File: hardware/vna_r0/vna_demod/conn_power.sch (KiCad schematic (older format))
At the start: 7 parts

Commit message: work on vna r0 schematics
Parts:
- added C? (x2): 22 uF, symbol CP_Small
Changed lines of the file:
@@
 LIBS:conn_sma_2gnd
 LIBS:conn_sma
+LIBS:txco
+LIBS:nb3n551
+LIBS:hmc475
+LIBS:trf37b73
 LIBS:vna_demod-cache
 EELAYER 25 0
@@
 Wire Wire Line
 	7300 4000 7500 4000
+$Comp
+L CP_Small C?
+U 1 1 5940338C
+P 5650 5000
+F 0 "C?" H 5660 5070 50  0000 L CNN
+F 1 "22 uF" H 5660 4920 50  0000 L CNN
+F 2 "" H 5650 5000 50  0001 C CNN
+F 3 "" H 5650 5000 50  0001 C CNN
+	1    5650 5000
+	1    0    0    -1
+$EndComp
+$Comp
+L CP_Small C?
+U 1 1 59403410
+P 6200 5000
+F 0 "C?" H 6210 5070 50  0000 L CNN
+F 1 "22 uF" H 6210 4920 50  0000 L CNN
+F 2 "" H 6200 5000 50  0001 C CNN
+F 3 "" H 6200 5000 50  0001 C CNN
+	1    6200 5000
+	1    0    0    -1
+$EndComp
 $EndSCHEMATC

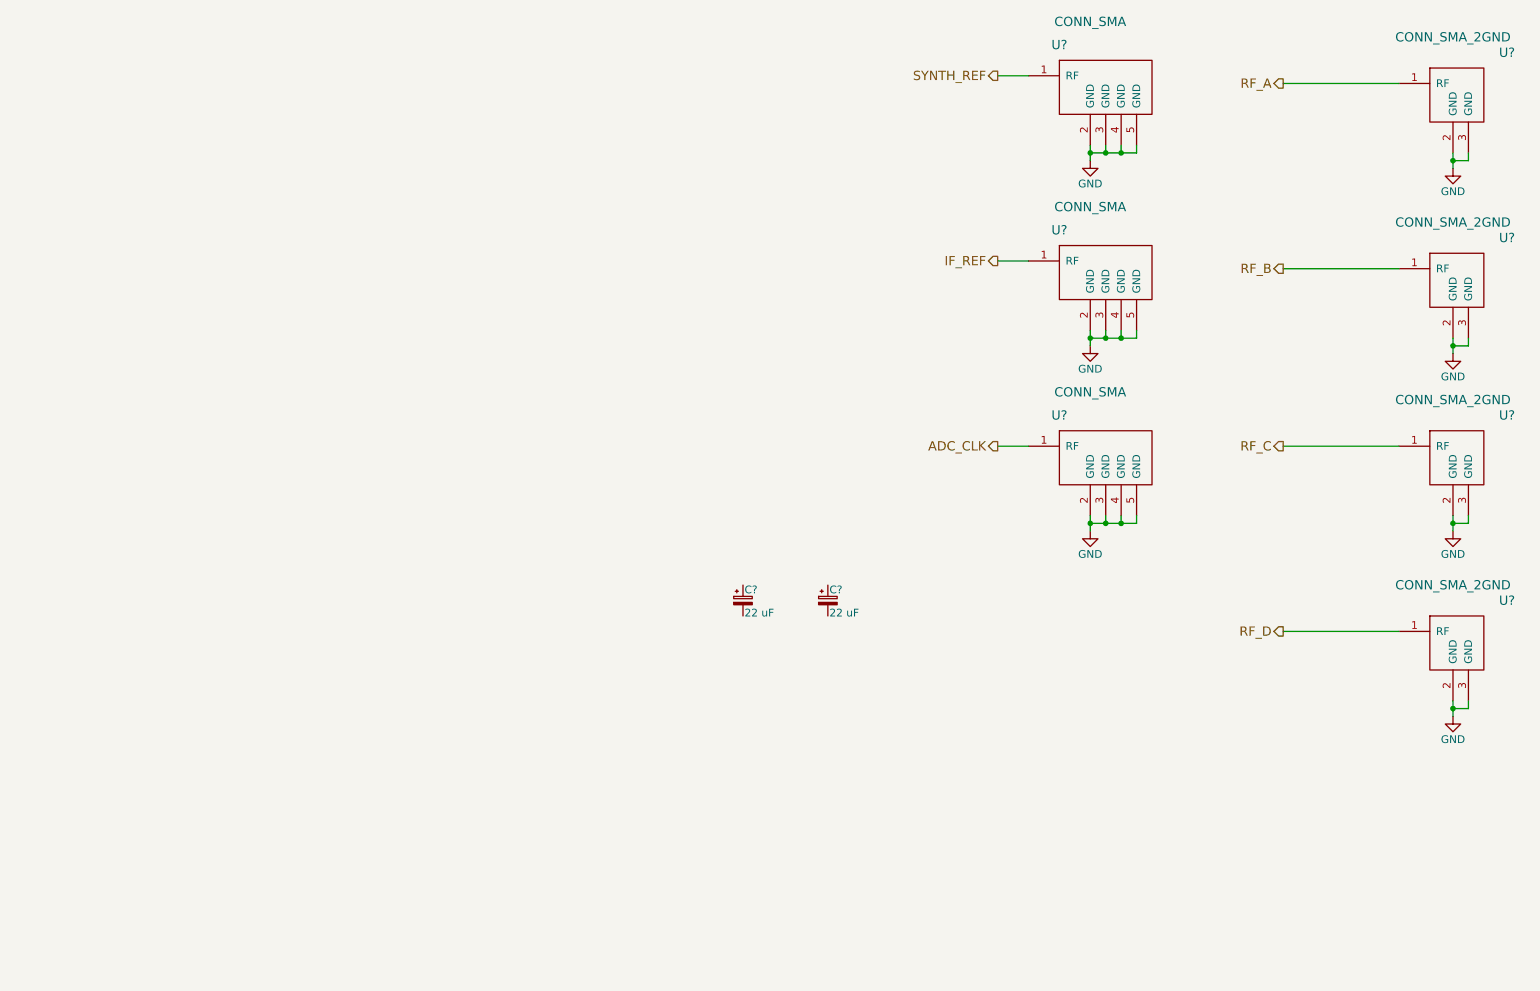
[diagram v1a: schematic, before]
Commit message: finished vna r0 demod schematic
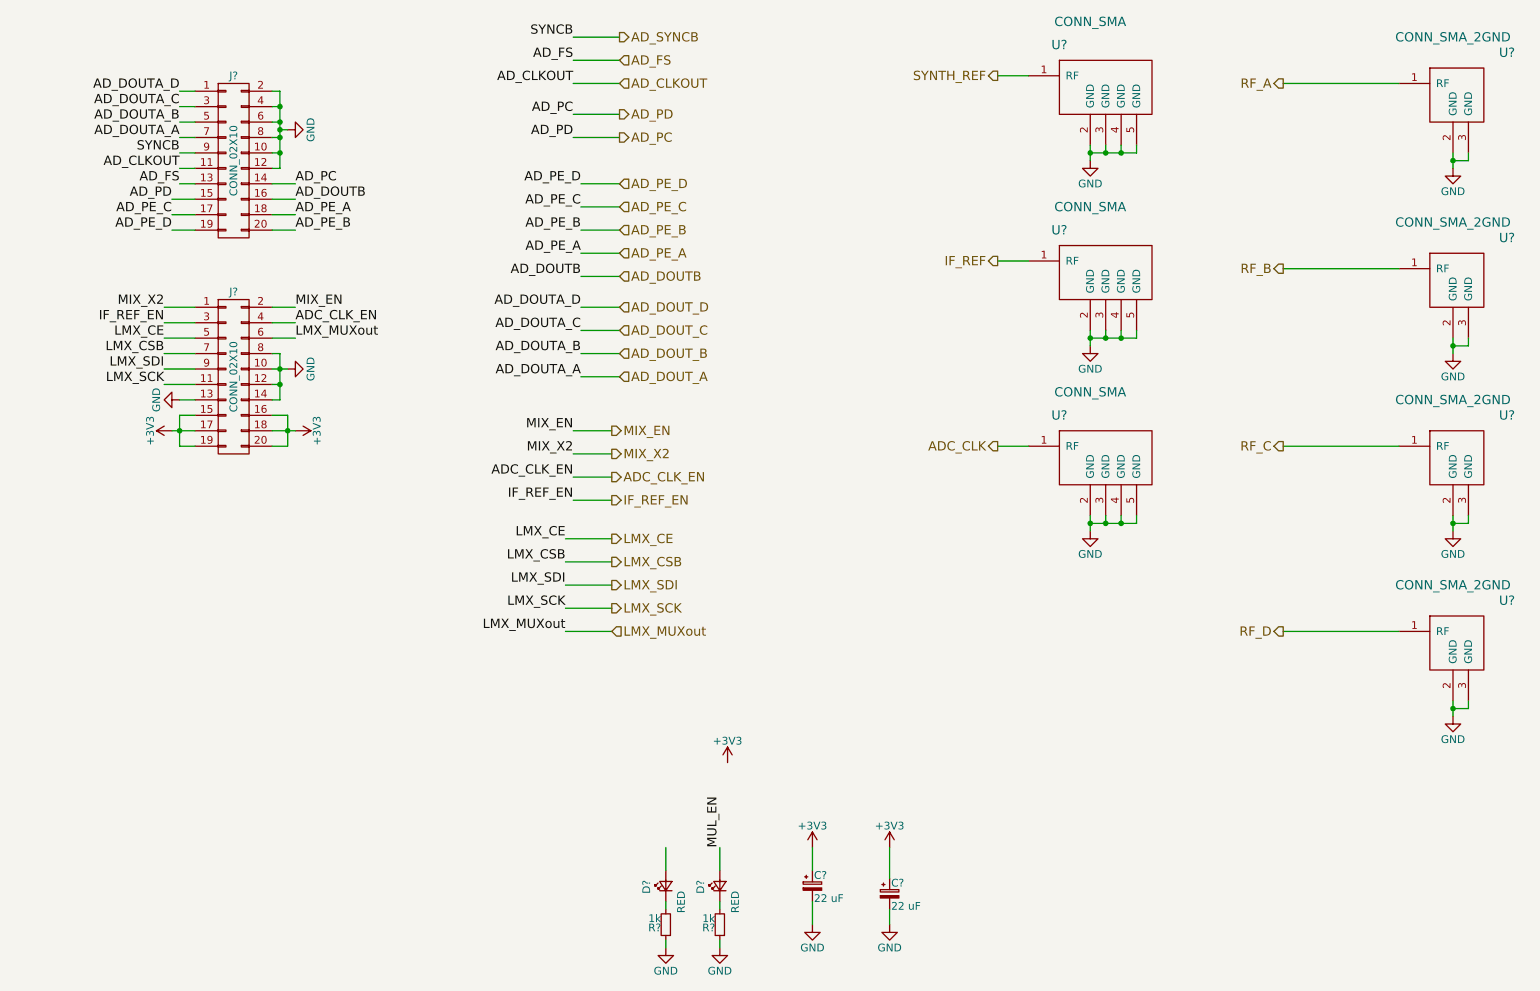
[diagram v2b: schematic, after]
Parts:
- added D? (x2): RED, symbol LED_Small
- added J? (x2): CONN_02X10, symbol CONN_02X10
- added R? (x2): 1k, symbol R_Small
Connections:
- net GND: now also C?.2, C?.2, J?.10 (P10), J?.10 (P10), J?.12 (P12), J?.12 (P12), J?.13 (P13), J?.14 (P14), J?.2 (P2), J?.4 (P4), J?.6 (P6), J?.8 (P8), J?.8 (P8), R?.1, R?.1
- net +3V3: now reaches C?.1
- net +3V3: now also C?.1, J?.15 (P15), J?.16 (P16), J?.17 (P17), J?.18 (P18), J?.19 (P19), J?.20 (P20)
- new net: D?.1 (K), R?.2 (x2)
- new net ADC_CLK_EN: J?.4 (P4)
- new net AD_CLKOUT: J?.11 (P11)
- new net AD_DOUTB: J?.16 (P16)
- new net AD_DOUT_A: J?.7 (P7)
- new net AD_DOUT_B: J?.5 (P5)
- new net AD_DOUT_C: J?.3 (P3)
- new net AD_DOUT_D: J?.1 (P1)
- new net AD_FS: J?.13 (P13)
- new net AD_PC: J?.14 (P14), J?.15 (P15)
- new net AD_PE_A: J?.18 (P18)
- new net AD_PE_B: J?.20 (P20)
- new net AD_PE_C: J?.17 (P17)
- new net AD_PE_D: J?.19 (P19)
- new net AD_SYNCB: J?.9 (P9)
- new net IF_REF_EN: J?.3 (P3)
- new net LMX_CE: J?.5 (P5)
- new net LMX_CSB: J?.7 (P7)
- new net LMX_MUXout: J?.6 (P6)
- new net LMX_SCK: J?.11 (P11)
- new net LMX_SDI: J?.9 (P9)
- new net MIX_EN: J?.2 (P2)
- new net MIX_X2: J?.1 (P1)
- new net MUL_EN: D?.2 (A)
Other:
- moved on the sheet: C?

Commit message: footprint assignment on vna r0
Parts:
- C401, C402: renamed from C?; footprint (none) -> Capacitors_SMD:c_elec_10x10
- D401, D402: renamed from D?; footprint (none) -> LEDs:LED_0603
- J401, J402: renamed from J?; footprint (none) -> Connect:IDC_Header_Straight_20pins
- R401, R402: renamed from R?; footprint (none) -> Resistors_SMD:R_0402
- U401, U402, U403: renamed from U?; footprint (none) -> vna_footprints:732511150_sma_thin
- U404, U405, U406, U407: renamed from U?; footprint (none) -> vna_footprints:SMA_901-10512_30MIL_OSHFR408_CPW_LAUNCH
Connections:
- net +3V3: now also D401.2 (A)

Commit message: started component placement on demod
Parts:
- removed C401: 22 uF, Capacitors_SMD:c_elec_10x10, symbol CP_Small
- added H401, H402, H403, H404: MOUNTING_HOLE, Mounting_Holes:MountingHole_2-7mm, symbol MOUNTING_HOLE
- added U408: mounting_box, vna_footprints:snail, symbol mounting_box
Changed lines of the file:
@@
 LIBS:hmc475
 LIBS:trf37b73
+LIBS:mounting_hole
+LIBS:mounting_box
 LIBS:vna_demod-cache
 EELAYER 25 0
@@
 F 3 "" H 7900 4550 50  0001 C CNN
 	1    7900 4550
-	1    0    0    -1
-$EndComp
-$Comp
-L CP_Small C401
-U 1 1 5940338C
-P 6100 6850
-F 0 "C401" H 6110 6920 50  0000 L CNN
-F 1 "22 uF" H 6110 6770 50  0000 L CNN
-F 2 "Capacitors_SMD:c_elec_10x10" H 6100 6850 50  0001 C CNN
-F 3 "" H 6100 6850 50  0001 C CNN
-	1    6100 6850
 	1    0    0    -1
 $EndComp
@@
 	4550 1500 4850 1500
 $Comp
-L +3V3 #PWR0101
-U 1 1 5940A9FF
-P 6100 6600
-F 0 "#PWR0101" H 6100 6450 50  0001 C CNN
-F 1 "+3V3" H 6100 6740 50  0000 C CNN
-F 2 "" H 6100 6600 50  0001 C CNN
-F 3 "" H 6100 6600 50  0001 C CNN
-	1    6100 6600
-	1    0    0    -1
-$EndComp
-Wire Wire Line
-	6100 6600 6100 6750
-$Comp
-L GND #PWR0102
-U 1 1 5940AB07
-P 6100 7100
-F 0 "#PWR0102" H 6100 6850 50  0001 C CNN
-F 1 "GND" H 6100 6950 50  0000 C CNN
-F 2 "" H 6100 7100 50  0001 C CNN
-F 3 "" H 6100 7100 50  0001 C CNN
-	1    6100 7100
-	1    0    0    -1
-$EndComp
-Wire Wire Line
-	6100 6950 6100 7100
-$Comp
 L +3V3 #PWR0103
 U 1 1 5940AB90
@@
 	1    0    0    -1
 $EndComp
+$Comp
+L MOUNTING_HOLE H401
+U 1 1 594735C1
+P 1350 4800
+F 0 "H401" H 1050 4850 60  0000 C CNN
+F 1 "MOUNTING_HOLE" H 1350 4950 60  0000 C CNN
+F 2 "Mounting_Holes:MountingHole_2-7mm" H 1350 4800 60  0001 C CNN
+F 3 "" H 1350 4800 60  0000 C CNN
+	1    1350 4800
+	1    0    0    -1
+$EndComp
+$Comp
+L MOUNTING_HOLE H402
+U 1 1 59473612
+P 1350 5150
+F 0 "H402" H 1050 5200 60  0000 C CNN
+F 1 "MOUNTING_HOLE" H 1350 5300 60  0000 C CNN
+F 2 "Mounting_Holes:MountingHole_2-7mm" H 1350 5150 60  0001 C CNN
+F 3 "" H 1350 5150 60  0000 C CNN
+	1    1350 5150
+	1    0    0    -1
+$EndComp
+$Comp
+L MOUNTING_HOLE H403
+U 1 1 59473689
+P 1400 5450
+F 0 "H403" H 1100 5500 60  0000 C CNN
+F 1 "MOUNTING_HOLE" H 1400 5600 60  0000 C CNN
+F 2 "Mounting_Holes:MountingHole_2-7mm" H 1400 5450 60  0001 C CNN
+F 3 "" H 1400 5450 60  0000 C CNN
+	1    1400 5450
+	1    0    0    -1
+$EndComp
+$Comp
+L MOUNTING_HOLE H404
+U 1 1 594736E5
+P 1400 5800
+F 0 "H404" H 1100 5850 60  0000 C CNN
+F 1 "MOUNTING_HOLE" H 1400 5950 60  0000 C CNN
+F 2 "Mounting_Holes:MountingHole_2-7mm" H 1400 5800 60  0001 C CNN
+F 3 "" H 1400 5800 60  0000 C CNN
+	1    1400 5800
+	1    0    0    -1
+$EndComp
+$Comp
+L mounting_box U408
+U 1 1 5947398E
+P 2000 6800
+F 0 "U408" H 2000 6800 60  0000 C CNN
+F 1 "mounting_box" H 1950 6950 60  0000 C CNN
+F 2 "vna_footprints:snail" H 2000 6800 60  0001 C CNN
+F 3 "" H 2000 6800 60  0000 C CNN
+	1    2000 6800
+	1    0    0    -1
+$EndComp

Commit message: work on vna r0 layout
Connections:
- net MUL_EN is gone; now on net MIX_EN: D402.2 (A)
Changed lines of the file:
@@
 	1    0    0    -1
 $EndComp
-Text Label 5500 6600 1    60   ~ 0
-MUL_EN
 Text Label 4550 3900 2    60   ~ 0
 MIX_EN
@@
 	1    0    0    -1
 $EndComp
+Text Label 5500 6600 1    60   ~ 0
+MIX_EN
 $EndSCHEMATC

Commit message: started on routing demod for vna r0
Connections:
- net LMX_CE: now also J402.11 (P11); no longer J402.5 (P5)
- net LMX_CSB: now also J402.9 (P9); no longer J402.7 (P7)
- net LMX_SCK: now also J402.5 (P5); no longer J402.11 (P11)
- net LMX_SDI: now also J402.7 (P7); no longer J402.9 (P9)
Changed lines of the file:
@@
 $EndComp
 $Comp
-L GND #PWR092
+L GND #PWR093
 U 1 1 5941528F
 P 10250 2200
-F 0 "#PWR092" H 10250 1950 50  0001 C CNN
+F 0 "#PWR093" H 10250 1950 50  0001 C CNN
 F 1 "GND" H 10250 2050 50  0000 C CNN
 F 2 "" H 10250 2200 50  0001 C CNN
@@
 $EndComp
 $Comp
-L GND #PWR093
+L GND #PWR094
 U 1 1 5941535D
 P 10250 3400
-F 0 "#PWR093" H 10250 3150 50  0001 C CNN
+F 0 "#PWR094" H 10250 3150 50  0001 C CNN
 F 1 "GND" H 10250 3250 50  0000 C CNN
 F 2 "" H 10250 3400 50  0001 C CNN
@@
 $EndComp
 $Comp
-L GND #PWR094
+L GND #PWR095
 U 1 1 5941544E
 P 10250 4550
-F 0 "#PWR094" H 10250 4300 50  0001 C CNN
+F 0 "#PWR095" H 10250 4300 50  0001 C CNN
 F 1 "GND" H 10250 4400 50  0000 C CNN
 F 2 "" H 10250 4550 50  0001 C CNN
@@
 $EndComp
 $Comp
-L GND #PWR095
+L GND #PWR096
 U 1 1 5941545F
 P 10250 5750
-F 0 "#PWR095" H 10250 5500 50  0001 C CNN
+F 0 "#PWR096" H 10250 5500 50  0001 C CNN
 F 1 "GND" H 10250 5600 50  0000 C CNN
 F 2 "" H 10250 5750 50  0001 C CNN
@@
 $EndComp
 $Comp
-L GND #PWR096
+L GND #PWR097
 U 1 1 5941587D
 P 7900 2150
-F 0 "#PWR096" H 7900 1900 50  0001 C CNN
+F 0 "#PWR097" H 7900 1900 50  0001 C CNN
 F 1 "GND" H 7900 2000 50  0000 C CNN
 F 2 "" H 7900 2150 50  0001 C CNN
@@
 $EndComp
 $Comp
-L GND #PWR097
+L GND #PWR098
 U 1 1 594159DD
 P 7900 3350
-F 0 "#PWR097" H 7900 3100 50  0001 C CNN
+F 0 "#PWR098" H 7900 3100 50  0001 C CNN
 F 1 "GND" H 7900 3200 50  0000 C CNN
 F 2 "" H 7900 3350 50  0001 C CNN
@@
 $EndComp
 $Comp
-L GND #PWR098
+L GND #PWR099
 U 1 1 59415A72
 P 7900 4550
-F 0 "#PWR098" H 7900 4300 50  0001 C CNN
+F 0 "#PWR099" H 7900 4300 50  0001 C CNN
 F 1 "GND" H 7900 4400 50  0000 C CNN
 F 2 "" H 7900 4550 50  0001 C CNN
@@
 $EndComp
 $Comp
-L GND #PWR099
+L GND #PWR0100
 U 1 1 593F92FD
 P 5150 7250
-F 0 "#PWR099" H 5150 7000 50  0001 C CNN
+F 0 "#PWR0100" H 5150 7000 50  0001 C CNN
 F 1 "GND" H 5150 7100 50  0000 C CNN
 F 2 "" H 5150 7250 50  0001 C CNN
@@
 $EndComp
 $Comp
-L GND #PWR0100
+L GND #PWR0101
 U 1 1 593F9989
 P 5500 7250
-F 0 "#PWR0100" H 5500 7000 50  0001 C CNN
+F 0 "#PWR0101" H 5500 7000 50  0001 C CNN
 F 1 "GND" H 5500 7100 50  0000 C CNN
 F 2 "" H 5500 7250 50  0001 C CNN
@@
 	4550 1500 4850 1500
 $Comp
-L +3V3 #PWR0101
+L +3V3 #PWR0102
 U 1 1 5940AB90
 P 6600 6600
-F 0 "#PWR0101" H 6600 6450 50  0001 C CNN
+F 0 "#PWR0102" H 6600 6450 50  0001 C CNN
 F 1 "+3V3" H 6600 6740 50  0000 C CNN
 F 2 "" H 6600 6600 50  0001 C CNN
@@
 $EndComp
 $Comp
-L GND #PWR0102
+L GND #PWR0103
 U 1 1 5940ABC2
 P 6600 7100
-F 0 "#PWR0102" H 6600 6850 50  0001 C CNN
+F 0 "#PWR0103" H 6600 6850 50  0001 C CNN
 F 1 "GND" H 6600 6950 50  0000 C CNN
 F 2 "" H 6600 7100 50  0001 C CNN
@@
 	2000 2100 2100 2100
 $Comp
-L GND #PWR0103
+L GND #PWR0104
 U 1 1 5940F933
 P 2700 1950
-F 0 "#PWR0103" H 2700 1700 50  0001 C CNN
+F 0 "#PWR0104" H 2700 1700 50  0001 C CNN
 F 1 "GND" H 2700 1800 50  0000 C CNN
 F 2 "" H 2700 1950 50  0001 C CNN
@@
 Text Label 1900 3200 2    60   ~ 0
 IF_REF_EN
+Text Label 1900 3600 2    60   ~ 0
+LMX_CE
+Text Label 1900 3500 2    60   ~ 0
+LMX_CSB
+Text Label 1900 3400 2    60   ~ 0
+LMX_SDI
 Text Label 1900 3300 2    60   ~ 0
-LMX_CE
-Text Label 1900 3400 2    60   ~ 0
-LMX_CSB
-Text Label 1900 3500 2    60   ~ 0
-LMX_SDI
-Text Label 1900 3600 2    60   ~ 0
 LMX_SCK
 Text Label 2750 3300 0    60   ~ 0
@@
 	1900 3400 2100 3400
 $Comp
-L GND #PWR0104
+L GND #PWR0105
 U 1 1 59410F35
 P 2700 3500
-F 0 "#PWR0104" H 2700 3250 50  0001 C CNN
+F 0 "#PWR0105" H 2700 3250 50  0001 C CNN
 F 1 "GND" H 2700 3350 50  0000 C CNN
 F 2 "" H 2700 3500 50  0001 C CNN
@@
 	1900 3600 2100 3600
 $Comp
-L +3V3 #PWR0105
+L +3V3 #PWR0106
 U 1 1 594112F7
 P 2750 3900
-F 0 "#PWR0105" H 2750 3750 50  0001 C CNN
+F 0 "#PWR0106" H 2750 3750 50  0001 C CNN
 F 1 "+3V3" H 2750 4040 50  0000 C CNN
 F 2 "" H 2750 3900 50  0001 C CNN
@@
 Connection ~ 2650 3600
 $Comp
-L GND #PWR0106
+L GND #PWR0107
 U 1 1 594114D4
 P 2000 3700
-F 0 "#PWR0106" H 2000 3450 50  0001 C CNN
+F 0 "#PWR0107" H 2000 3450 50  0001 C CNN
 F 1 "GND" H 2000 3550 50  0000 C CNN
 F 2 "" H 2000 3700 50  0001 C CNN
@@
 Connection ~ 2700 3900
 $Comp
-L +3V3 #PWR0107
+L +3V3 #PWR0108
 U 1 1 59411794
 P 1950 3900
-F 0 "#PWR0107" H 1950 3750 50  0001 C CNN
+F 0 "#PWR0108" H 1950 3750 50  0001 C CNN
 F 1 "+3V3" H 1950 4040 50  0000 C CNN
 F 2 "" H 1950 3900 50  0001 C CNN
@@
 	2000 4000 2100 4000
 $Comp
-L +3V3 #PWR0108
+L +3V3 #PWR0109
 U 1 1 593F95B6
 P 5150 6600
-F 0 "#PWR0108" H 5150 6450 50  0001 C CNN
+F 0 "#PWR0109" H 5150 6450 50  0001 C CNN
 F 1 "+3V3" H 5150 6740 50  0000 C CNN
 F 2 "" H 5150 6600 50  0001 C CNN

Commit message: routing on demod, almost done..
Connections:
- net AD_DOUTB: now also J401.14 (P14); no longer J401.16 (P16)
- net AD_PC: no longer J401.14 (P14)
- new net AD_PD: J401.16 (P16)
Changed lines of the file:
@@
 AD_PE_C
 Text Label 4550 2000 2    60   ~ 0
+AD_PC
+Text Label 4550 1850 2    60   ~ 0
 AD_PD
-Text Label 4550 1850 2    60   ~ 0
-AD_PC
 Text Label 4600 3250 2    60   ~ 0
 AD_DOUTA_C
@@
 Wire Wire Line
 	2750 2500 2600 2500
+Text Label 2750 2300 0    60   ~ 0
+AD_DOUTB
+Wire Wire Line
+	2750 2400 2600 2400
 Text Label 2750 2400 0    60   ~ 0
-AD_DOUTB
-Wire Wire Line
-	2750 2400 2600 2400
+AD_PD
+Wire Wire Line
+	1950 2400 2100 2400
 Text Label 1950 2400 2    60   ~ 0
-AD_PD
-Wire Wire Line
-	1950 2400 2100 2400
-Text Label 2750 2300 0    60   ~ 0
 AD_PC
 Wire Wire Line
